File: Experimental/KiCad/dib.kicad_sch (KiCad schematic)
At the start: 7 parts, among them X10 1001878410201TLF, X11 77313-802-20LF, X12 77313-802-20LF, X13 10018783-10101TLF, X14 5051102091, X15 TBP03R1-350-10BE

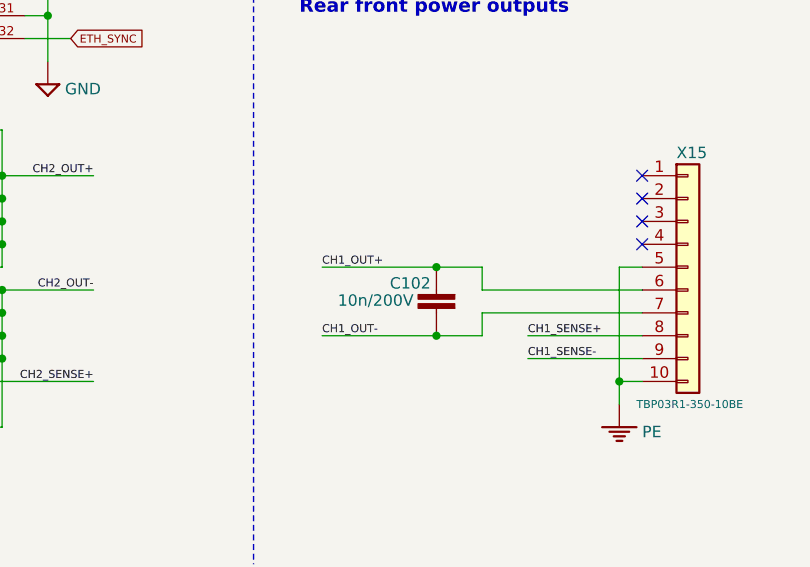
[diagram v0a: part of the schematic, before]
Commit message: Replace 3V3 jumper for H7 CM5 with PMOS sw
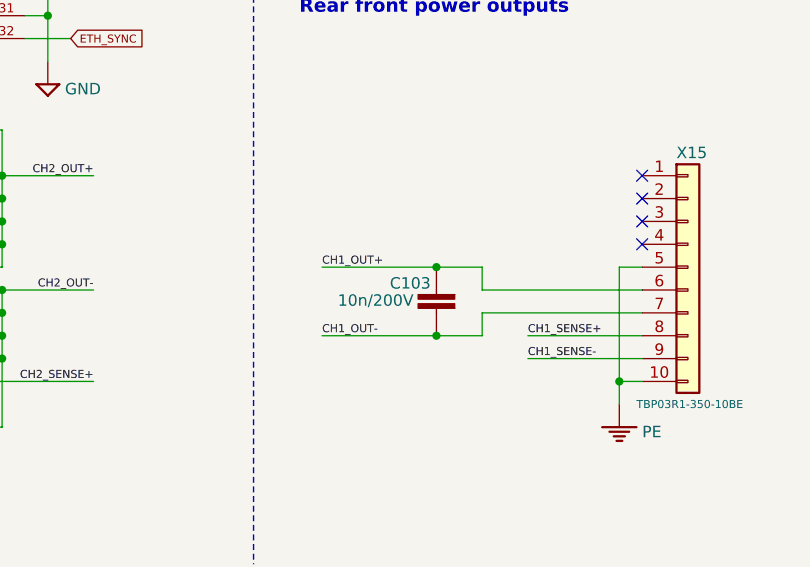
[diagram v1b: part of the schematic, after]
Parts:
- renumbered C102 to C103
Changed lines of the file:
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@@
 		(on_board yes)
 		(dnp no)
-		(property "Reference" "#SUPPLY064"
+		(property "Reference" "#SUPPLY065"
 			(at 81.28 109.22 0)
 			(effects
@@
 			(project "BB3plus MCU test board"
 				(path "/1df84e4f-233a-4f72-9418-c0020706bb76/57aee854-8c94-4105-bcce-97e3d73b363b"
-					(reference "#SUPPLY064")
+					(reference "#SUPPLY065")
 					(unit 1)
 				)
@@
 		(on_board yes)
 		(dnp no)
-		(property "Reference" "#+3V028"
+		(property "Reference" "#+3V029"
 			(at 83.82 60.96 0)
 			(effects
@@
 			(project "BB3plus MCU test board"
 				(path "/1df84e4f-233a-4f72-9418-c0020706bb76/57aee854-8c94-4105-bcce-97e3d73b363b"
-					(reference "#+3V028")
+					(reference "#+3V029")
 					(unit 1)
 				)
@@
 		(on_board yes)
 		(dnp no)
-		(property "Reference" "#SUPPLY067"
+		(property "Reference" "#SUPPLY068"
 			(at 157.48 109.22 0)
 			(effects
@@
 			(project "BB3plus MCU test board"
 				(path "/1df84e4f-233a-4f72-9418-c0020706bb76/57aee854-8c94-4105-bcce-97e3d73b363b"
-					(reference "#SUPPLY067")
+					(reference "#SUPPLY068")
 					(unit 1)
 				)
@@
 		(on_board yes)
 		(dnp no)
-		(property "Reference" "C102"
+		(property "Reference" "C103"
 			(at 200.025 132.08 0)
 			(effects
@@
 			(project "BB3plus MCU test board"
 				(path "/1df84e4f-233a-4f72-9418-c0020706bb76/57aee854-8c94-4105-bcce-97e3d73b363b"
-					(reference "C102")
+					(reference "C103")
 					(unit 1)
 				)
@@
 		(on_board yes)
 		(dnp no)
-		(property "Reference" "#SUPPLY066"
+		(property "Reference" "#SUPPLY067"
 			(at 119.38 50.8 0)
 			(effects
@@
 			(project "BB3plus MCU test board"
 				(path "/1df84e4f-233a-4f72-9418-c0020706bb76/57aee854-8c94-4105-bcce-97e3d73b363b"
-					(reference "#SUPPLY066")
+					(reference "#SUPPLY067")
 					(unit 1)
 				)
@@
 		(on_board yes)
 		(dnp no)
-		(property "Reference" "#SUPPLY065"
+		(property "Reference" "#SUPPLY066"
 			(at 83.82 50.8 0)
 			(effects
@@
 			(project "BB3plus MCU test board"
 				(path "/1df84e4f-233a-4f72-9418-c0020706bb76/57aee854-8c94-4105-bcce-97e3d73b363b"
-					(reference "#SUPPLY065")
+					(reference "#SUPPLY066")
 					(unit 1)
 				)
@@
 		(on_board yes)
 		(dnp no)
-		(property "Reference" "#+3V031"
+		(property "Reference" "#+3V032"
 			(at 165.1 30.48 0)
 			(effects
@@
 			(project "BB3plus MCU test board"
 				(path "/1df84e4f-233a-4f72-9418-c0020706bb76/57aee854-8c94-4105-bcce-97e3d73b363b"
-					(reference "#+3V031")
+					(reference "#+3V032")
 					(unit 1)
 				)
@@
 		(on_board yes)
 		(dnp no)
-		(property "Reference" "#+3V030"
+		(property "Reference" "#+3V031"
 			(at 162.56 63.5 0)
 			(effects
@@
 			(project "BB3plus MCU test board"
 				(path "/1df84e4f-233a-4f72-9418-c0020706bb76/57aee854-8c94-4105-bcce-97e3d73b363b"
-					(reference "#+3V030")
+					(reference "#+3V031")
 					(unit 1)
 				)
@@
 		(on_board yes)
 		(dnp no)
-		(property "Reference" "#SUPPLY068"
+		(property "Reference" "#SUPPLY069"
 			(at 160.02 50.8 0)
 			(effects
@@
 			(project "BB3plus MCU test board"
 				(path "/1df84e4f-233a-4f72-9418-c0020706bb76/57aee854-8c94-4105-bcce-97e3d73b363b"
-					(reference "#SUPPLY068")
+					(reference "#SUPPLY069")
 					(unit 1)
 				)
@@
 		(on_board yes)
 		(dnp no)
-		(property "Reference" "#+3V032"
+		(property "Reference" "#+3V033"
 			(at 218.44 78.74 0)
 			(effects
@@
 			(project "BB3plus MCU test board"
 				(path "/1df84e4f-233a-4f72-9418-c0020706bb76/57aee854-8c94-4105-bcce-97e3d73b363b"
-					(reference "#+3V032")
+					(reference "#+3V033")
 					(unit 1)
 				)
@@
 		(on_board yes)
 		(dnp no)
-		(property "Reference" "#+3V029"
+		(property "Reference" "#+3V030"
 			(at 88.9 30.48 0)
 			(effects
@@
 			(project "BB3plus MCU test board"
 				(path "/1df84e4f-233a-4f72-9418-c0020706bb76/57aee854-8c94-4105-bcce-97e3d73b363b"
-					(reference "#+3V029")
+					(reference "#+3V030")
 					(unit 1)
 				)
@@
 		(on_board yes)
 		(dnp no)
-		(property "Reference" "#SUPPLY063"
+		(property "Reference" "#SUPPLY064"
 			(at 43.18 50.8 0)
 			(effects
@@
 			(project "BB3plus MCU test board"
 				(path "/1df84e4f-233a-4f72-9418-c0020706bb76/57aee854-8c94-4105-bcce-97e3d73b363b"
-					(reference "#SUPPLY063")
-					(unit 1)
-				)
+					(reference "#SUPPLY064")
+					(unit 1)
+				)

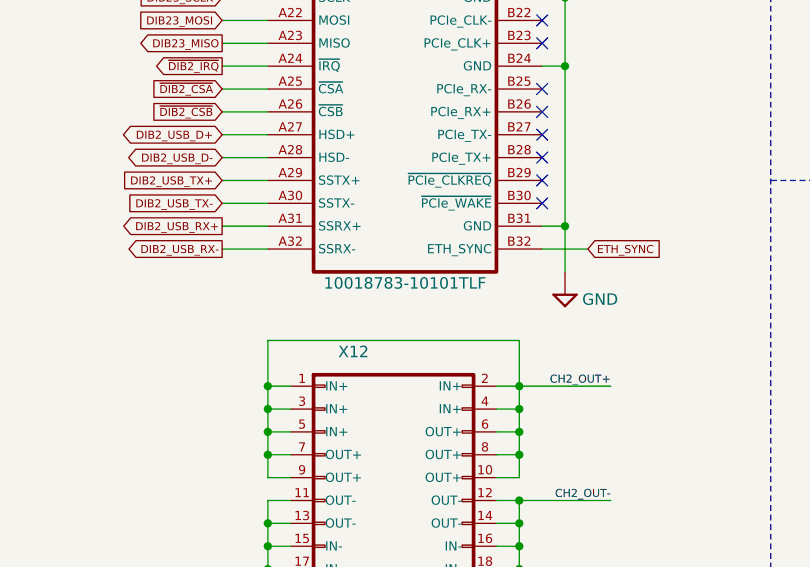
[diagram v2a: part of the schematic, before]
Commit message: Power switch modified
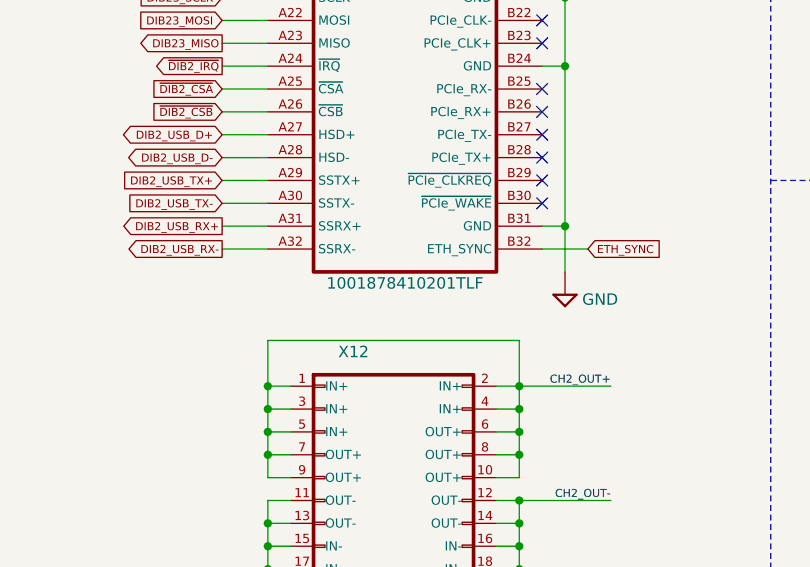
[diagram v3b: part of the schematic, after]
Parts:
- X13: value 10018783-10101TLF -> 1001878410201TLF; Mouser 649-18783-10101TLF -> 649-1001878410201TLF; TME 1001878310101T-0 -> 1001878410201T-0
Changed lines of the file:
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@@
 	(title_block
 		(title "${project_name}")
-		(date "2025-10-21")
+		(date "2025-10-23")
 		(rev "${project_version}")
 		(company "${project_creator}")
@@
 		(on_board yes)
 		(dnp no)
-		(property "Reference" "#SUPPLY065"
+		(property "Reference" "#SUPPLY064"
 			(at 81.28 109.22 0)
 			(effects
@@
 			(project "BB3plus MCU test board"
 				(path "/1df84e4f-233a-4f72-9418-c0020706bb76/57aee854-8c94-4105-bcce-97e3d73b363b"
-					(reference "#SUPPLY065")
+					(reference "#SUPPLY064")
 					(unit 1)
 				)
@@
 		(on_board yes)
 		(dnp no)
-		(property "Reference" "#SUPPLY068"
+		(property "Reference" "#SUPPLY067"
 			(at 157.48 109.22 0)
 			(effects
@@
 			(project "BB3plus MCU test board"
 				(path "/1df84e4f-233a-4f72-9418-c0020706bb76/57aee854-8c94-4105-bcce-97e3d73b363b"
-					(reference "#SUPPLY068")
+					(reference "#SUPPLY067")
 					(unit 1)
 				)
@@
 		(on_board yes)
 		(dnp no)
-		(property "Reference" "#SUPPLY067"
+		(property "Reference" "#SUPPLY066"
 			(at 119.38 50.8 0)
 			(effects
@@
 			(project "BB3plus MCU test board"
 				(path "/1df84e4f-233a-4f72-9418-c0020706bb76/57aee854-8c94-4105-bcce-97e3d73b363b"
-					(reference "#SUPPLY067")
+					(reference "#SUPPLY066")
 					(unit 1)
 				)
@@
 		(on_board yes)
 		(dnp no)
-		(property "Reference" "#SUPPLY066"
+		(property "Reference" "#SUPPLY065"
 			(at 83.82 50.8 0)
 			(effects
@@
 			(project "BB3plus MCU test board"
 				(path "/1df84e4f-233a-4f72-9418-c0020706bb76/57aee854-8c94-4105-bcce-97e3d73b363b"
-					(reference "#SUPPLY066")
+					(reference "#SUPPLY065")
 					(unit 1)
 				)
@@
 		(on_board yes)
 		(dnp no)
-		(property "Reference" "#SUPPLY069"
+		(property "Reference" "#SUPPLY068"
 			(at 160.02 50.8 0)
 			(effects
@@
 			(project "BB3plus MCU test board"
 				(path "/1df84e4f-233a-4f72-9418-c0020706bb76/57aee854-8c94-4105-bcce-97e3d73b363b"
-					(reference "#SUPPLY069")
+					(reference "#SUPPLY068")
 					(unit 1)
 				)
@@
 			)
 		)
-		(property "Value" "10018783-10101TLF"
+		(property "Value" "1001878410201TLF"
 			(at 139.7 107.95 0)
 			(effects
@@
 			)
 		)
-		(property "Mouser" "649-18783-10101TLF"
+		(property "Mouser" "649-1001878410201TLF"
 			(at 129.54 20.32 0)
 			(effects
@@
 			)
 		)
-		(property "TME" "1001878310101T-0"
+		(property "TME" "1001878410201T-0"
 			(at 129.54 20.32 0)
 			(effects
@@
 		(on_board yes)
 		(dnp no)
-		(property "Reference" "#SUPPLY064"
+		(property "Reference" "#SUPPLY063"
 			(at 43.18 50.8 0)
 			(effects
@@
 			(project "BB3plus MCU test board"
 				(path "/1df84e4f-233a-4f72-9418-c0020706bb76/57aee854-8c94-4105-bcce-97e3d73b363b"
-					(reference "#SUPPLY064")
+					(reference "#SUPPLY063")
 					(unit 1)
 				)
